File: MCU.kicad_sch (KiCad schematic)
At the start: 18 parts, among them J10 ICSP, J11 PROG, SW1 RESET, U2 ATmega2560-16A, U3 CSTNE16M0V530000R0

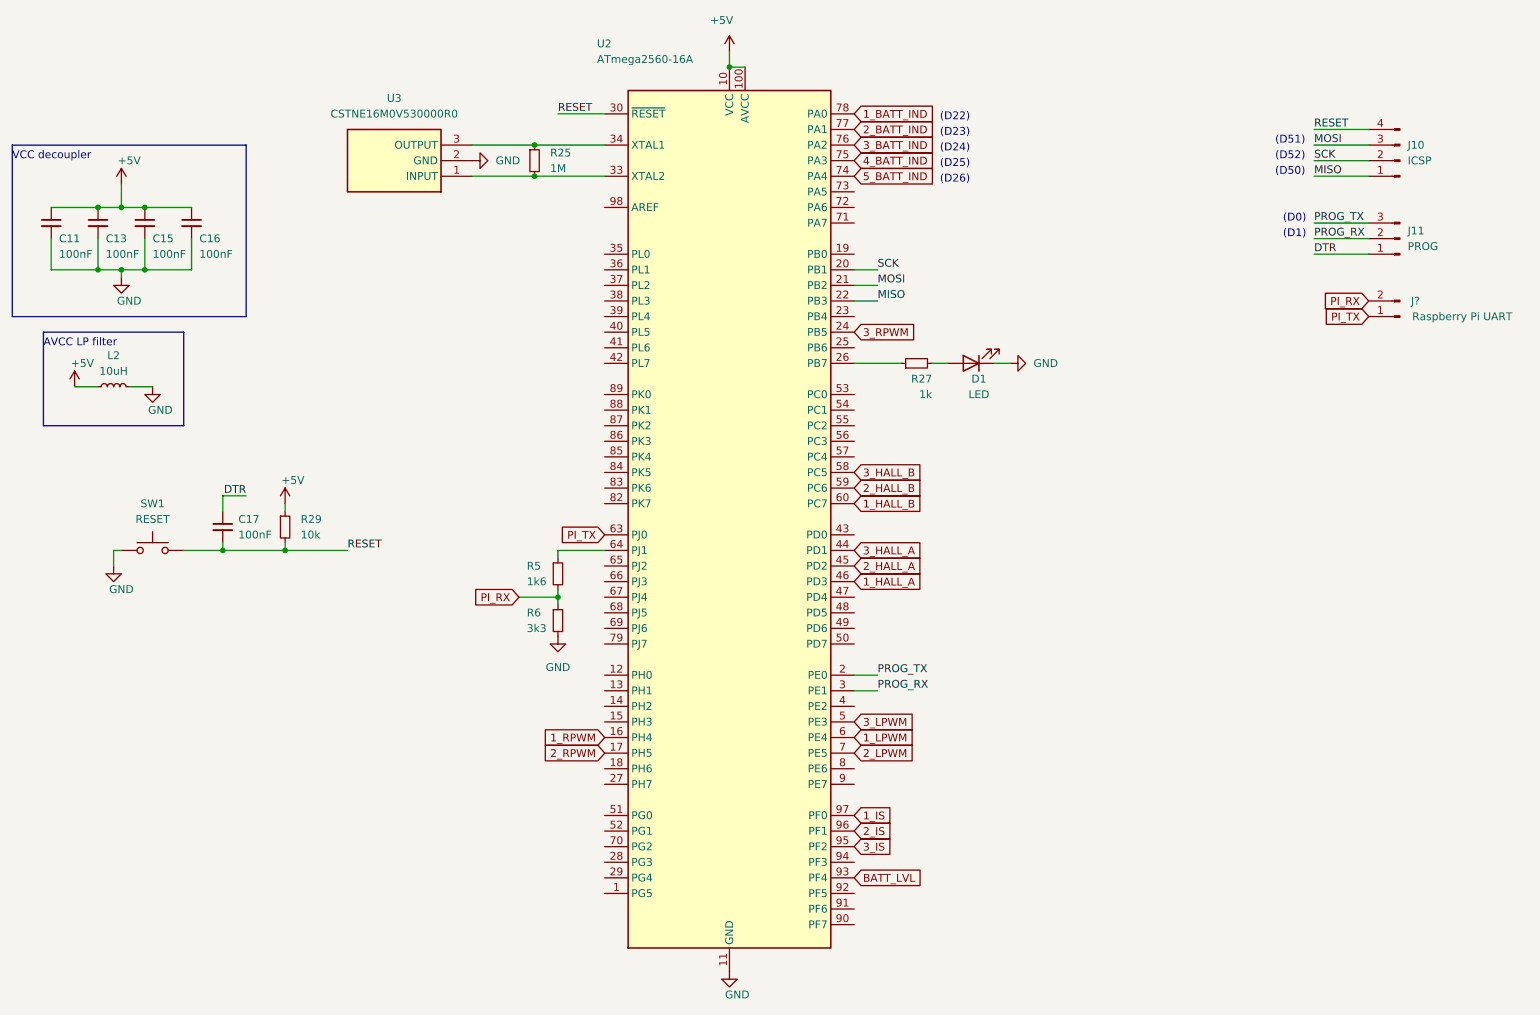
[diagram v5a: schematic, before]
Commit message: Completed full schematics
New features:
- extra 5V reg for handling camera current
- extra 12V reg for powering external LEDs
- added circuit for external emergency stop switch
- added some solder jumper for design flexibility
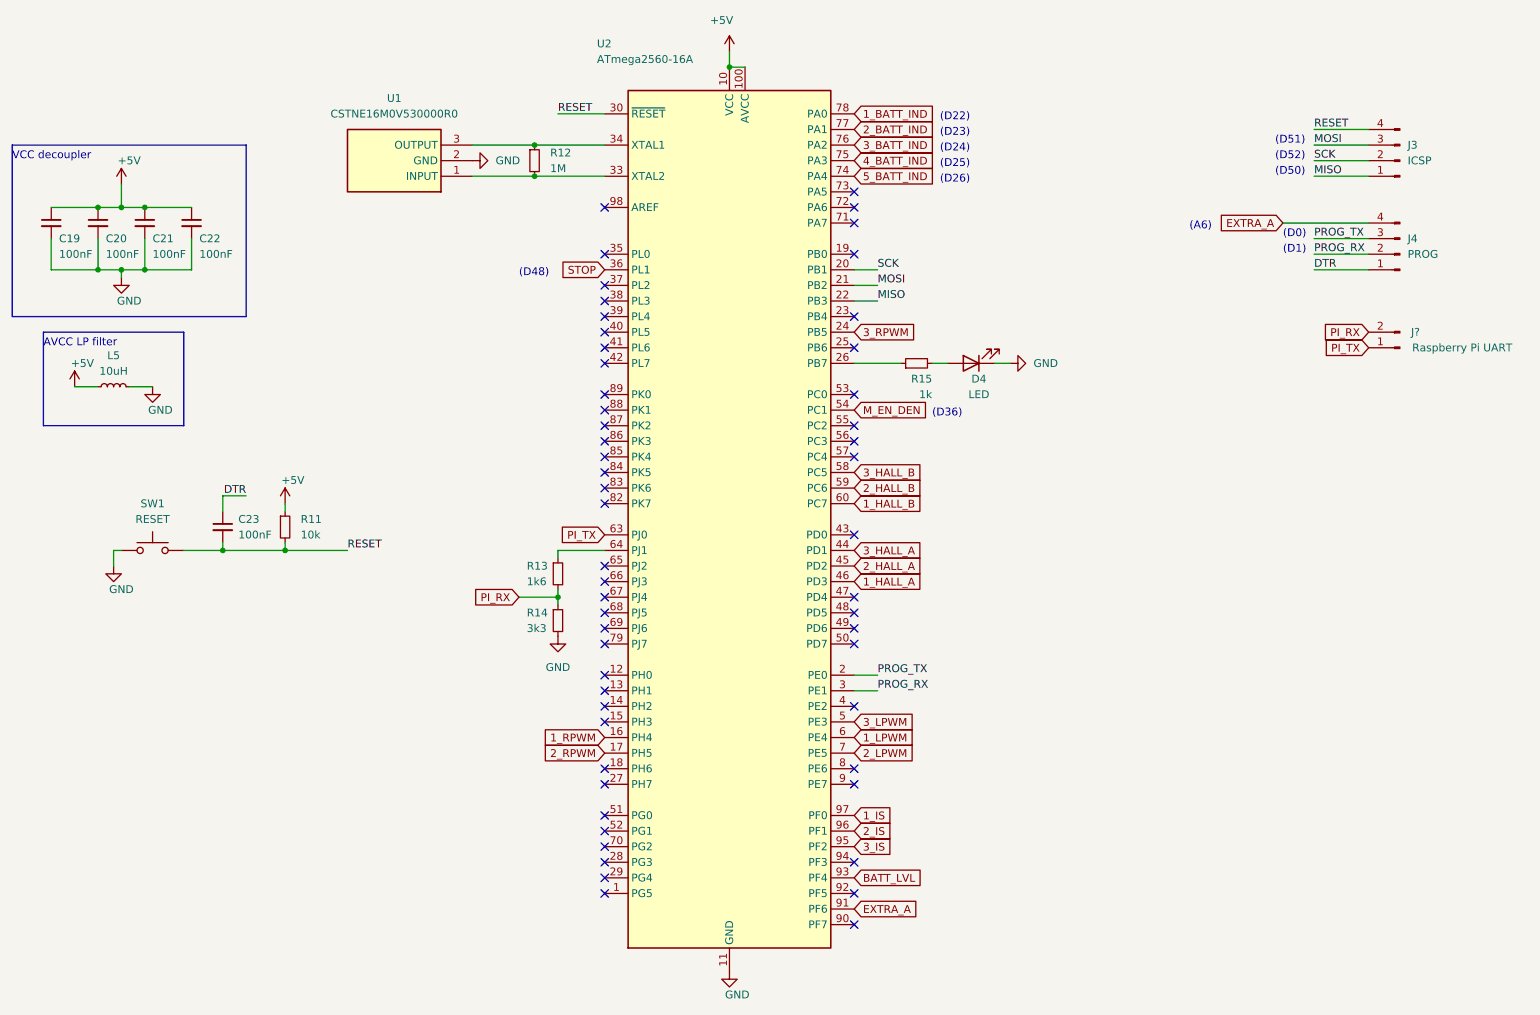
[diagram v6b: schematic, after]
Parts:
- removed J11: PROG, symbol Connector:Conn_01x03_Pin
- added J4: PROG, symbol Connector:Conn_01x04_Pin
- renumbered C11 to C19, C13 to C20, C15 to C21, C16 to C22, C17 to C23, D1 to D4, J10 to J3, L2 to L5, R29 to R11, R25 to R12, R5 to R13, R6 to R14, R27 to R15, U3 to U1
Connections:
- net DTR: now also J4.1 (Pin_1)
- net PROG_RX: now also J4.2 (Pin_2)
- net PROG_TX: now also J4.3 (Pin_3)
- net STOP: now reaches U2.36 (PL1)
- net M_EN_DEN: now reaches U2.54 (PC1)
- net EXTRA_A: now reaches U2.91 (PF6)
- net EXTRA_A: now also J4.4 (Pin_4)
- no-connect marks 0 -> 55
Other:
- note added: "(A6)"
- note added: "(D36)"
- note added: "(D48)"
- moved on the sheet: J?

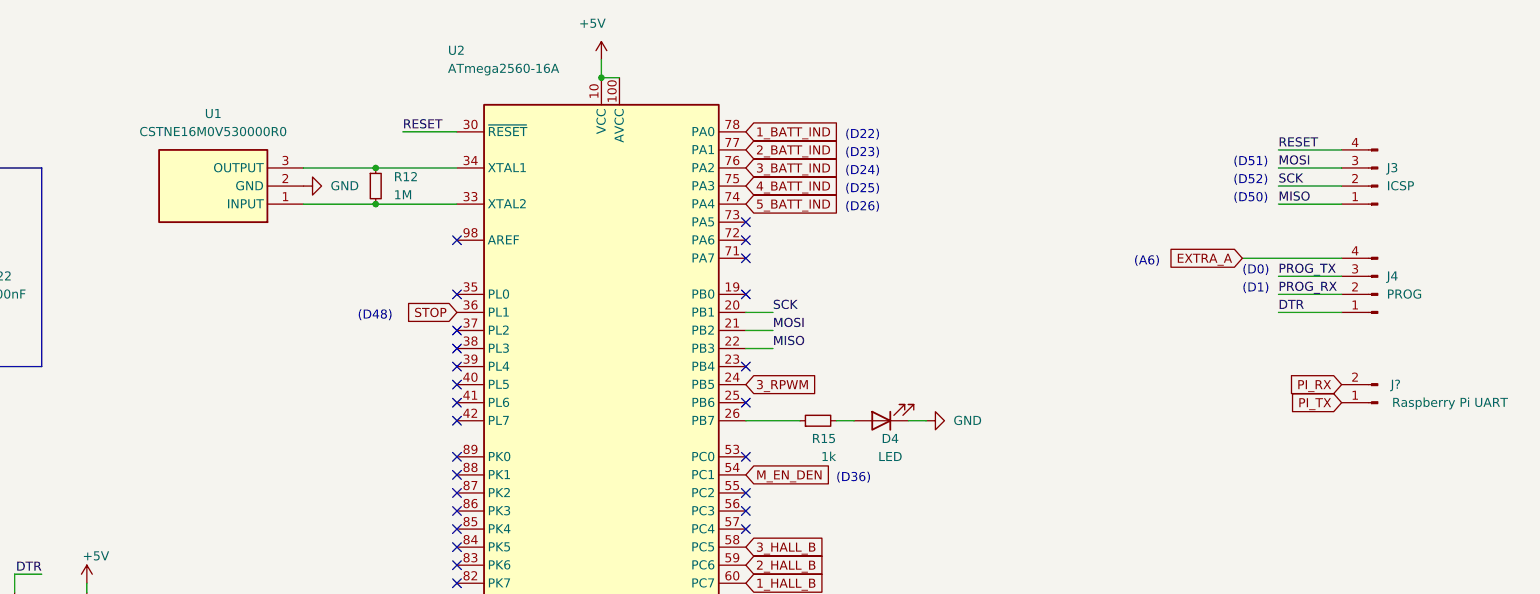
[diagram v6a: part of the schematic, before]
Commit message: completed footprint assignments
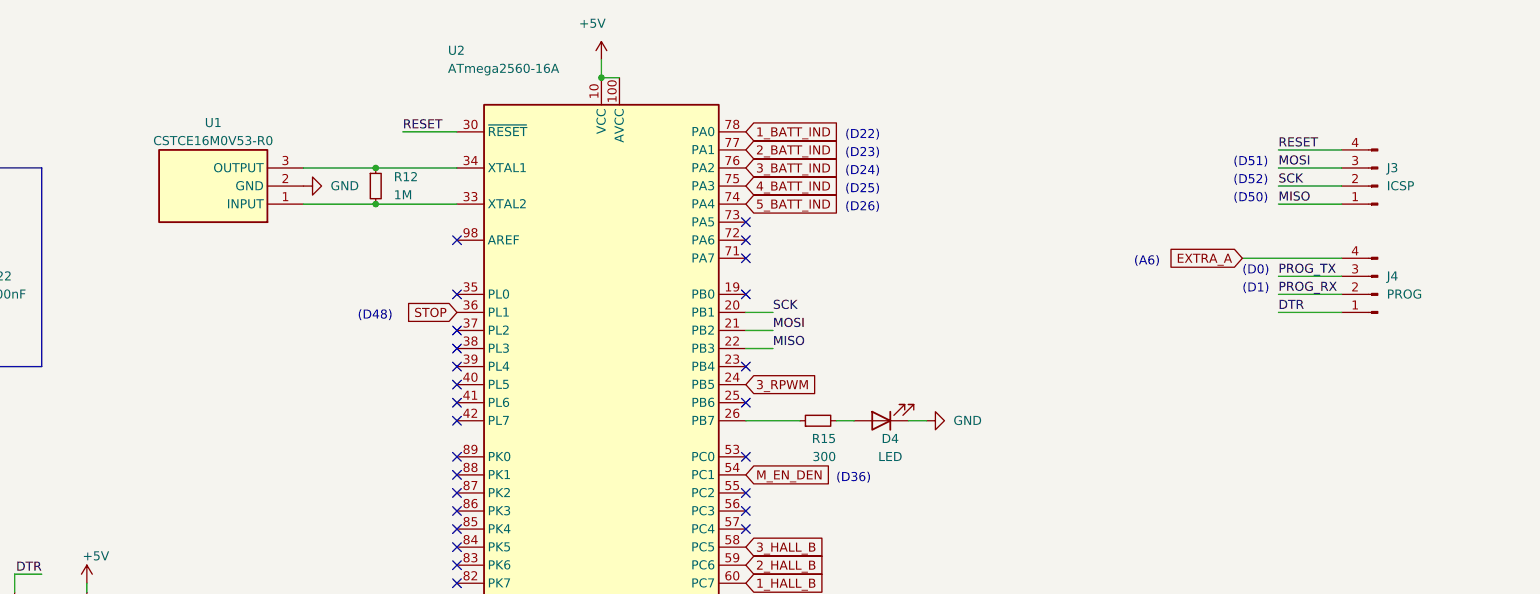
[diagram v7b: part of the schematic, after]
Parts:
- removed J?: Raspberry Pi UART, Connector_PinHeader_2.54mm:PinHeader_1x02_P2.54mm_Vertical, symbol Connector:Conn_01x02_Pin
- C19, C20, C21, C22, C23: footprint (none) -> Capacitor_SMD:C_0402_1005Metric
- D4: footprint (none) -> Diode_SMD:D_0805_2012Metric; Part No. (none) -> NCD0805Y1
- J3, J4: footprint (none) -> Connector_PinHeader_2.54mm:PinHeader_2x02_P2.54mm_Vertical
- L5: footprint (none) -> Inductor_SMD:L_0805_2012Metric; Part No. (none) -> MLZ2012M100HT000
- R11: footprint (none) -> Resistor_SMD:R_0402_1005Metric; Part No. (none) -> AC0402FR-0710KL
- R12: footprint (none) -> Resistor_SMD:R_0402_1005Metric
- R15: value 1k -> 300; footprint (none) -> Resistor_SMD:R_0603_1608Metric_Pad0.98x0.95mm_HandSolder; Part No. (none) -> CR0603-FX-3000ELF
- SW1: footprint (none) -> Connector_PinHeader_2.54mm:PinHeader_1x02_P2.54mm_Vertical
- U1: value CSTNE16M0V530000R0 -> CSTCE16M0V53-R0; footprint SamacSys_Parts:CSTNE16M0V530000R0 -> SamacSys_Parts:CSTCE16M0V53R0
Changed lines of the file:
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@@
-    )
-  )
-  (global_label "PI_RX" (shape input) (at 234.95 67.31 180) (fields_autoplaced)
-    (effects (font (size 1.27 1.27)) (justify right))
-    (property "Intersheetrefs" "${INTERSHEET_REFS}" (at 226.6429 67.31 0)
-      (effects (font (size 1.27 1.27)) (justify right) hide)
     )
   )
@@
     )
   )
-  (global_label "PI_TX" (shape input) (at 234.95 69.85 180) (fields_autoplaced)
-    (effects (font (size 1.27 1.27)) (justify right))
-    (property "Intersheetrefs" "${INTERSHEET_REFS}" (at 226.9453 69.85 0)
-      (effects (font (size 1.27 1.27)) (justify right) hide)
-    )
-  )
   (symbol (lib_id "power:+5V") (at 24.13 76.2 0) (unit 1)
     (in_bom yes) (on_board yes) (dnp no)
@@
       (effects (font (size 1.27 1.27)) (justify left))
     )
-    (property "Footprint" "" (at 99.06 39.37 0)
+    (property "Footprint" "Resistor_SMD:R_0402_1005Metric" (at 99.06 39.37 0)
       (effects (font (size 1.27 1.27)) hide)
     )
@@
       (effects (font (size 1.27 1.27)))
     )
-    (property "Footprint" "" (at 170.18 72.39 0)
+    (property "Footprint" "Diode_SMD:D_0805_2012Metric" (at 170.18 72.39 0)
       (effects (font (size 1.27 1.27)) hide)
     )
@@
       (effects (font (size 1.27 1.27)) hide)
     )
+    (property "Part No." "NCD0805Y1" (at 170.18 72.39 0)
+      (effects (font (size 1.27 1.27)) hide)
+    )
     (pin "1")
     (pin "2")
@@
       (effects (font (size 1.27 1.27)) (justify left))
     )
-    (property "Footprint" "" (at 27.94 49.53 0)
+    (property "Footprint" "Capacitor_SMD:C_0402_1005Metric" (at 27.94 49.53 0)
       (effects (font (size 1.27 1.27)) hide)
     )
@@
       (effects (font (size 1.27 1.27)) (justify right))
     )
-    (property "Footprint" "" (at 240.03 39.37 0)
+    (property "Footprint" "Connector_PinHeader_2.54mm:PinHeader_2x02_P2.54mm_Vertical" (at 240.03 39.37 0)
       (effects (font (size 1.27 1.27)) hide)
     )
@@
       (effects (font (size 1.27 1.27)) (justify left))
     )
-    (property "Footprint" "" (at 43.18 49.53 0)
+    (property "Footprint" "Capacitor_SMD:C_0402_1005Metric" (at 43.18 49.53 0)
       (effects (font (size 1.27 1.27)) hide)
     )
@@
       (effects (font (size 1.27 1.27)) (justify left))
     )
-    (property "Footprint" "" (at 20.32 49.53 0)
+    (property "Footprint" "Capacitor_SMD:C_0402_1005Metric" (at 20.32 49.53 0)
       (effects (font (size 1.27 1.27)) hide)
     )
@@
       (effects (font (size 1.27 1.27)) (justify left))
     )
-    (property "Value" "1k" (at 163.83 77.47 90)
-      (effects (font (size 1.27 1.27)) (justify left))
-    )
-    (property "Footprint" "" (at 161.29 72.39 0)
+    (property "Value" "300" (at 163.83 77.47 90)
+      (effects (font (size 1.27 1.27)) (justify left))
+    )
+    (property "Footprint" "Resistor_SMD:R_0603_1608Metric_Pad0.98x0.95mm_HandSolder" (at 161.29 72.39 0)
       (effects (font (size 1.27 1.27)) hide)
     )
     (property "Datasheet" "~" (at 161.29 72.39 0)
+      (effects (font (size 1.27 1.27)) hide)
+    )
+    (property "Part No." "CR0603-FX-3000ELF" (at 161.29 72.39 90)
       (effects (font (size 1.27 1.27)) hide)
     )
@@
       (effects (font (size 1.27 1.27)))
     )
-    (property "Footprint" "" (at 36.83 97.79 0)
+    (property "Footprint" "Connector_PinHeader_2.54mm:PinHeader_1x02_P2.54mm_Vertical" (at 36.83 97.79 0)
       (effects (font (size 1.27 1.27)) hide)
     )
@@
       (effects (font (size 1.27 1.27)) (justify left))
     )
-    (property "Footprint" "" (at 58.42 99.06 0)
+    (property "Footprint" "Resistor_SMD:R_0402_1005Metric" (at 58.42 99.06 0)
       (effects (font (size 1.27 1.27)) hide)
     )
@@
       (effects (font (size 1.27 1.27)) hide)
     )
+    (property "Part No." "AC0402FR-0710KL" (at 58.42 99.06 0)
+      (effects (font (size 1.27 1.27)) hide)
+    )
     (pin "1")
     (pin "2")
@@
         (path "/1df96114-eb1a-4ddf-9ea3-acd2b4d12bf3/89b185b8-71a2-451f-8308-7ae776af2b3f"
           (reference "#PWR027") (unit 1)
-        )
-      )
-    )
-  )
-  (symbol (lib_id "Connector:Conn_01x02_Pin") (at 240.03 69.85 180) (unit 1)
-    (in_bom yes) (on_board yes) (dnp no)
-    (property "Reference" "J?" (at 242.57 67.31 0)
-      (effects (font (size 1.27 1.27)))
-    )
-    (property "Value" "Raspberry Pi UART" (at 250.19 69.85 0)
-      (effects (font (size 1.27 1.27)))
-    )
-    (property "Footprint" "Connector_PinHeader_2.54mm:PinHeader_1x02_P2.54mm_Vertical" (at 240.03 69.85 0)
-      (effects (font (size 1.27 1.27)) hide)
-    )
-    (property "Datasheet" "~" (at 240.03 69.85 0)
-      (effects (font (size 1.27 1.27)) hide)
-    )
-    (pin "1")
-    (pin "2")
-    (instances
-      (project "rbc_circuits"
-        (path "/1df96114-eb1a-4ddf-9ea3-acd2b4d12bf3/6683f276-27a3-494e-84c3-353277da8be6"
-          (reference "J?") (unit 1)
-        )
-        (path "/1df96114-eb1a-4ddf-9ea3-acd2b4d12bf3/89b185b8-71a2-451f-8308-7ae776af2b3f"
-          (reference "J5") (unit 1)
         )
       )
@@
   (symbol (lib_id "SamacSys_Parts:CSTNE16M0V530000R0") (at 88.9 41.91 180) (unit 1)
     (in_bom yes) (on_board yes) (dnp no) (fields_autoplaced)
-    (property "Reference" "U1" (at 76.2 29.21 0)
-      (effects (font (size 1.27 1.27)))
-    )
-    (property "Value" "CSTNE16M0V530000R0" (at 76.2 31.75 0)
-      (effects (font (size 1.27 1.27)))
-    )
-    (property "Footprint" "SamacSys_Parts:CSTNE16M0V530000R0" (at 67.31 -53.01 0)
+    (property "Reference" "U1" (at 76.2 30.48 0)
+      (effects (font (size 1.27 1.27)))
+    )
+    (property "Value" "CSTCE16M0V53-R0" (at 76.2 33.02 0)
+      (effects (font (size 1.27 1.27)))
+    )
+    (property "Footprint" "SamacSys_Parts:CSTCE16M0V53R0" (at 67.31 -53.01 0)
       (effects (font (size 1.27 1.27)) (justify left top) hide)
     )
@@
       (effects (font (size 1.27 1.27)) (justify left))
     )
-    (property "Footprint" "" (at 35.56 49.53 0)
+    (property "Footprint" "Capacitor_SMD:C_0402_1005Metric" (at 35.56 49.53 0)
       (effects (font (size 1.27 1.27)) hide)
     )
@@
       (effects (font (size 1.27 1.27)) (justify left))
     )
-    (property "Footprint" "" (at 48.26 99.06 0)
+    (property "Footprint" "Capacitor_SMD:C_0402_1005Metric" (at 48.26 99.06 0)
       (effects (font (size 1.27 1.27)) hide)
     )
@@
       (effects (font (size 1.27 1.27)))
     )
-    (property "Footprint" "" (at 30.48 76.2 0)
+    (property "Footprint" "Inductor_SMD:L_0805_2012Metric" (at 30.48 76.2 0)
       (effects (font (size 1.27 1.27)) hide)
     )
     (property "Datasheet" "~" (at 30.48 76.2 0)
+      (effects (font (size 1.27 1.27)) hide)
+    )
+    (property "Part No." "MLZ2012M100HT000" (at 30.48 76.2 90)
       (effects (font (size 1.27 1.27)) hide)
     )
@@
       (effects (font (size 1.27 1.27)) (justify right))
     )
-    (property "Footprint" "" (at 240.03 54.61 0)
-      (effects (font (size 1.27 1.27)) hide)
-    )
+    (property "Footprint" "Connector_PinHeader_2.54mm:PinHeader_2x02_P2.54mm_Vertical" (at 240.03 54.61 0)
+      (effects (font (size 1.27 1.27)) hide)
+    )

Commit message: PCB initial commit
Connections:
- net DTR: no longer J4.1 (Pin_1)
- net EXTRA_A: no longer J4.4 (Pin_4)
- net PROG_RX: no longer J4.2 (Pin_2)
- net PROG_TX: no longer J4.3 (Pin_3)
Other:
- moved on the sheet: J4
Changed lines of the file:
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@@
   )
   (symbol (lib_id "SamacSys_Parts:CSTNE16M0V530000R0") (at 88.9 41.91 180) (unit 1)
-    (in_bom yes) (on_board yes) (dnp no) (fields_autoplaced)
+    (in_bom yes) (on_board yes) (dnp no)
     (property "Reference" "U1" (at 76.2 30.48 0)
       (effects (font (size 1.27 1.27)))
@@
     )
   )
-  (symbol (lib_id "Connector:Conn_01x04_Pin") (at 240.03 54.61 180) (unit 1)
-    (in_bom yes) (on_board yes) (dnp no) (fields_autoplaced)
-    (property "Reference" "J4" (at 241.3 52.07 0)
+  (symbol (lib_id "Connector:Conn_01x04_Pin") (at 240.03 54.61 0) (mirror x) (unit 1)
+    (in_bom yes) (on_board yes) (dnp no)
+    (property "Reference" "J4" (at 238.76 52.07 0)
       (effects (font (size 1.27 1.27)) (justify right))
     )
-    (property "Value" "PROG" (at 241.3 54.61 0)
+    (property "Value" "PROG" (at 238.76 54.61 0)
       (effects (font (size 1.27 1.27)) (justify right))
     )
